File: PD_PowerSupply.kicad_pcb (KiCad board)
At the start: 2 copper layers, 5 parts, among them J1 USB4085-GF-A_REVA, Q1 STL6P3LLH6, Q2 STL6P3LLH6, U1 STUSB4500QTR, U2 ESP32-WROOM-32

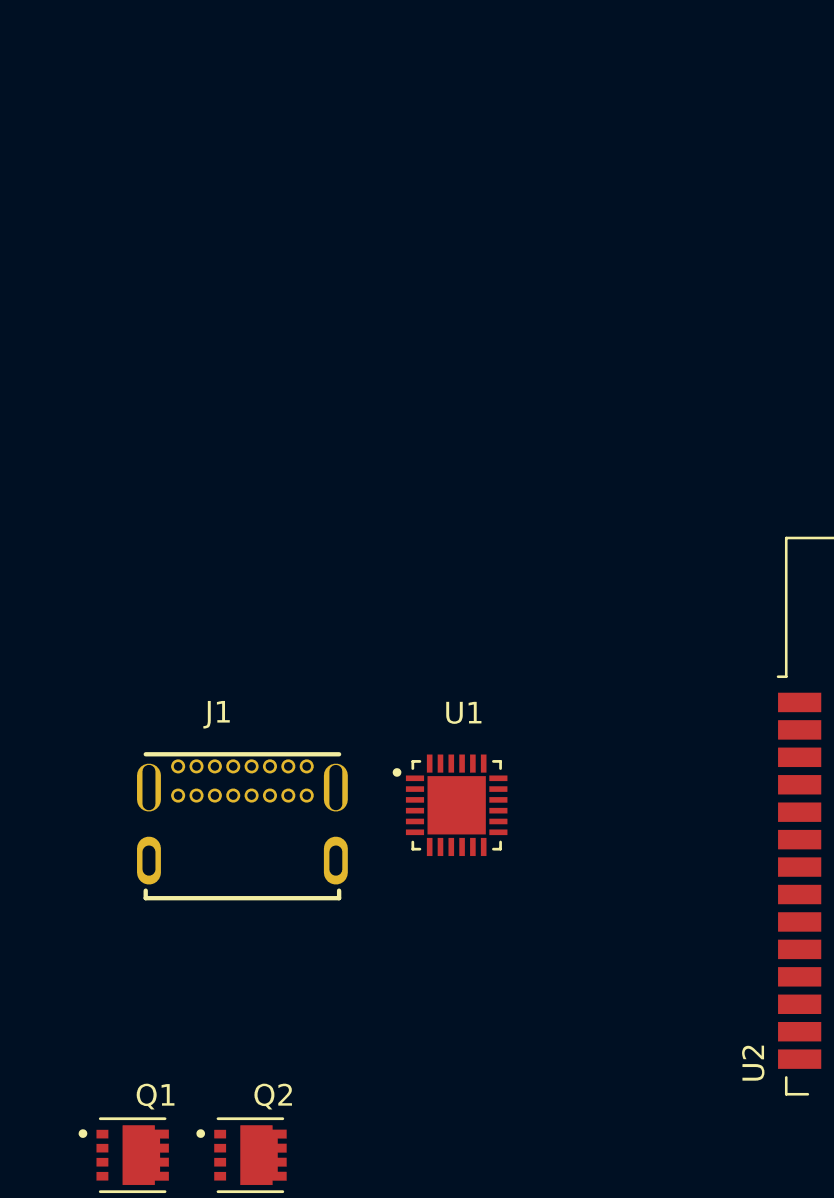
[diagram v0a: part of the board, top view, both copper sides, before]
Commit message: switched to linear chip
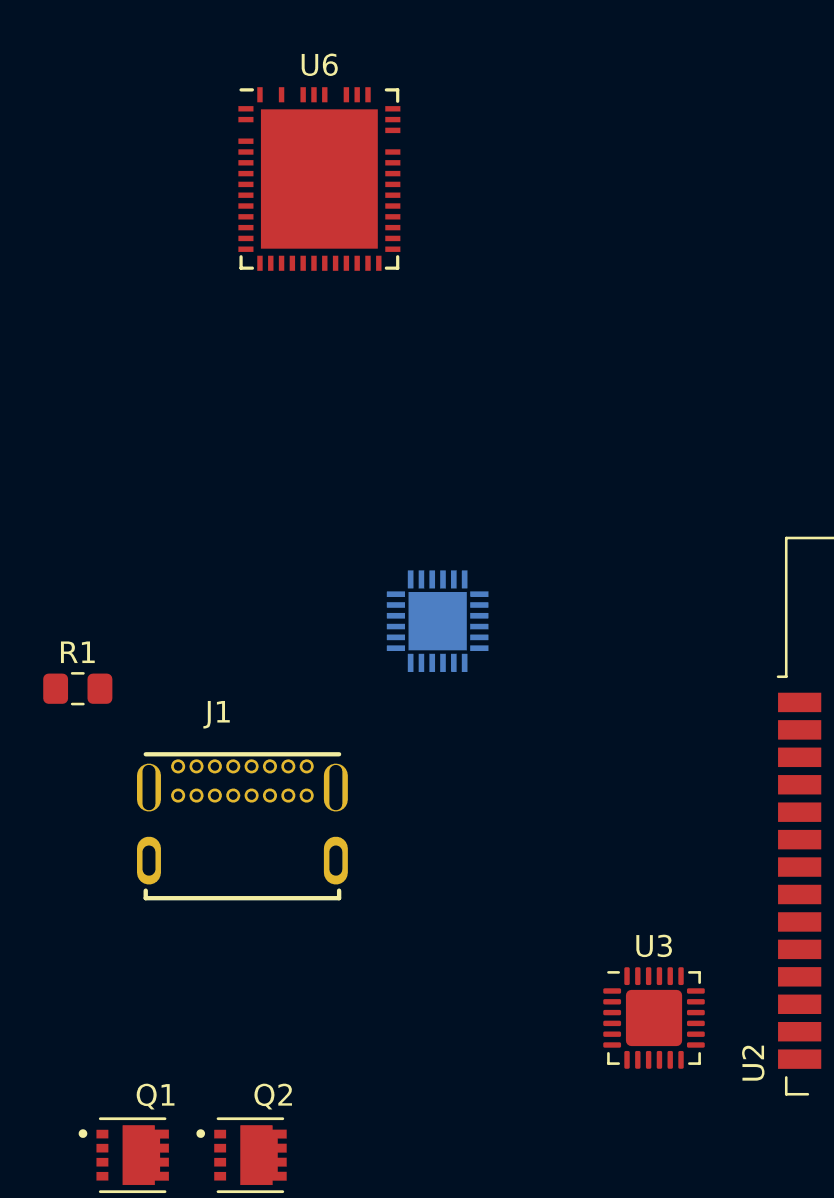
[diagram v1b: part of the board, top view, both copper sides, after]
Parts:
- added R1: 22k, Resistor_SMD:R_0805_2012Metric_Pad1.15x1.40mm_HandSolder, F.Cu at (59.7, 108.0)
- added U3: CP2102N, Package_DFN_QFN:QFN-24-1EP_4x4mm_P0.5mm_EP2.6x2.6mm, F.Cu at (86.4, 123.2)
- added U6: LTC3886, Package_DFN_QFN:Linear_UGK52_QFN-46-52, F.Cu at (70.9, 84.4)
- U1: moved to B.Cu
- moved U1 8.57 mm to (76.3, 104.8), turned to 90 degrees
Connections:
- net +12V renamed /vSINK
- net Net-(D1-Pad2) renamed VBUS
- U1 pad 1: Net-(J1-PadA5) -> Net-(JP1-Pad2)
- U1 pad 5: Net-(J1-PadB5) -> Net-(JP2-Pad2)
- U2 pad 1: Net-(U2-Pad1) -> GND
- U2 pad 15: Net-(U2-Pad1) -> GND
- U2 pad 2: Net-(U2-Pad2) -> +3V3
- U2 pad 38: Net-(U2-Pad1) -> GND
- U2 pad 39: Net-(U2-Pad1) -> GND
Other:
- rule via_min_drill: 0.3 -> 0.00254
- rule via_min_size: 0.4 -> 0.00254

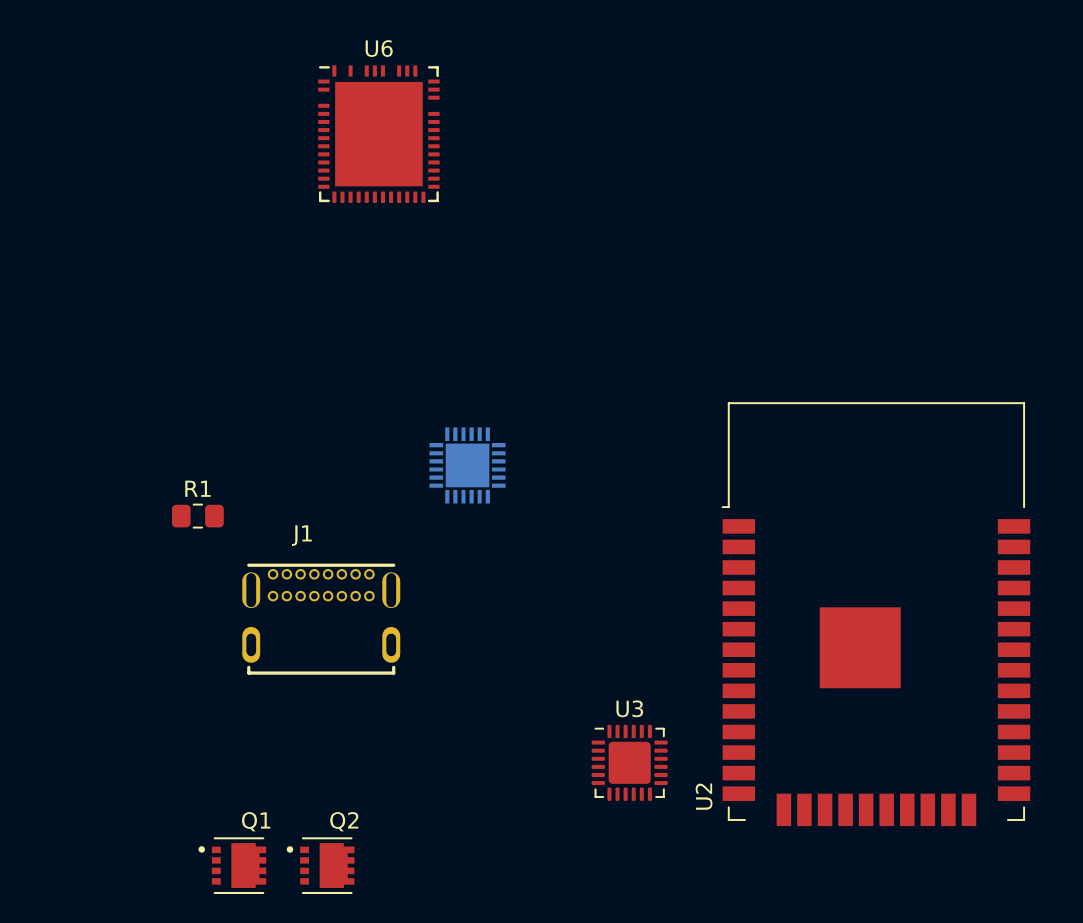
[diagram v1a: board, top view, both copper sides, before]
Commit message: switched to unswitched
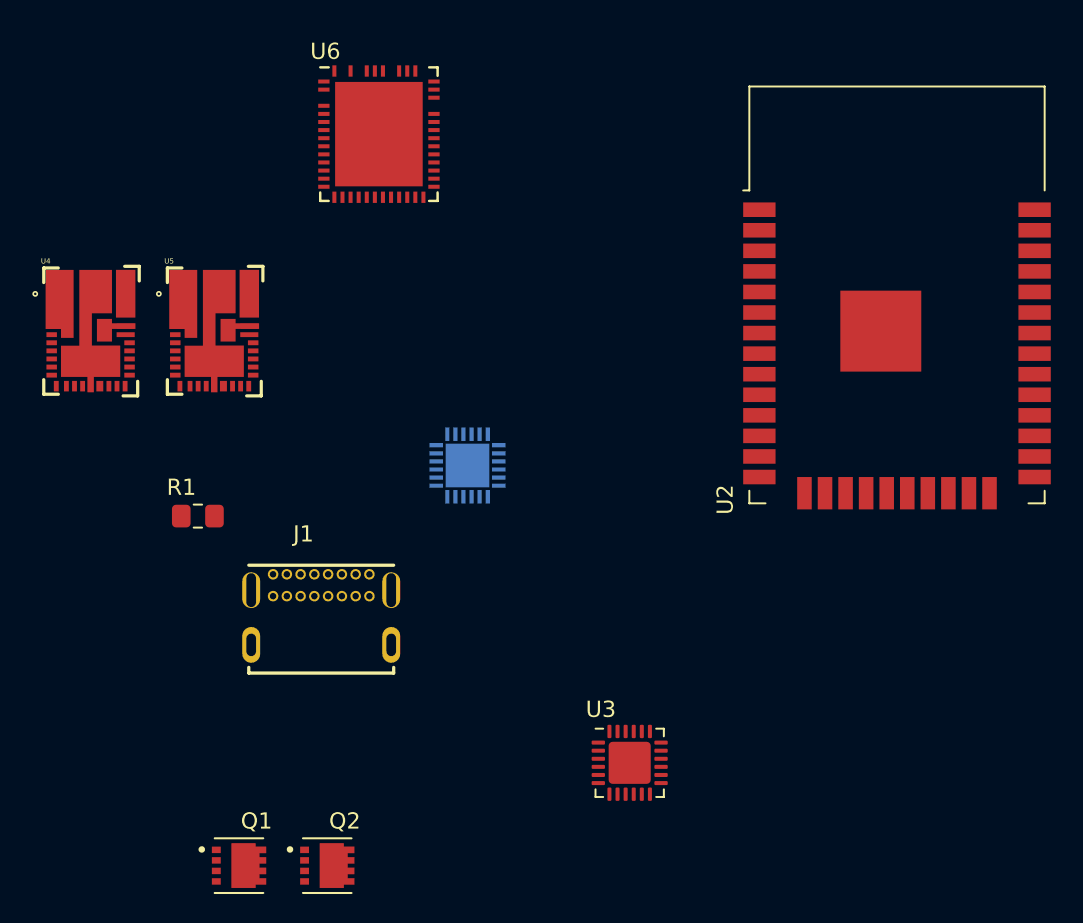
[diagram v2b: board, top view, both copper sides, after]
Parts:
- added U4: IR38062MTRPBF, IR38062MTRPBF:PQFN50P700X500X100-26N, F.Cu at (53.1, 96.5)
- added U5: IR38062MTRPBF, IR38062MTRPBF:PQFN50P700X500X100-26N, F.Cu at (60.7, 96.5)
- moved U2 19.6 mm to (102.9, 97.3)
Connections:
- U6 pad 53: Net-(U6-Pad53) -> GND
